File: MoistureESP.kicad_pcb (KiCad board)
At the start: 2 copper layers, 106 parts, among them J1 Conn_01x02_Pin, J2 Conn_MoisturePCB, J3 Conn_DS18B20, J4 Conn_01x06_Pin, J5 Conn_01x03_Pin, J7 USB4110-GF-A, Q1 SSM6K513NU-LF, Q10 SI7137DP-T1-GE3, Q2 SSM6K513NU-LF, Q3 2N7002W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

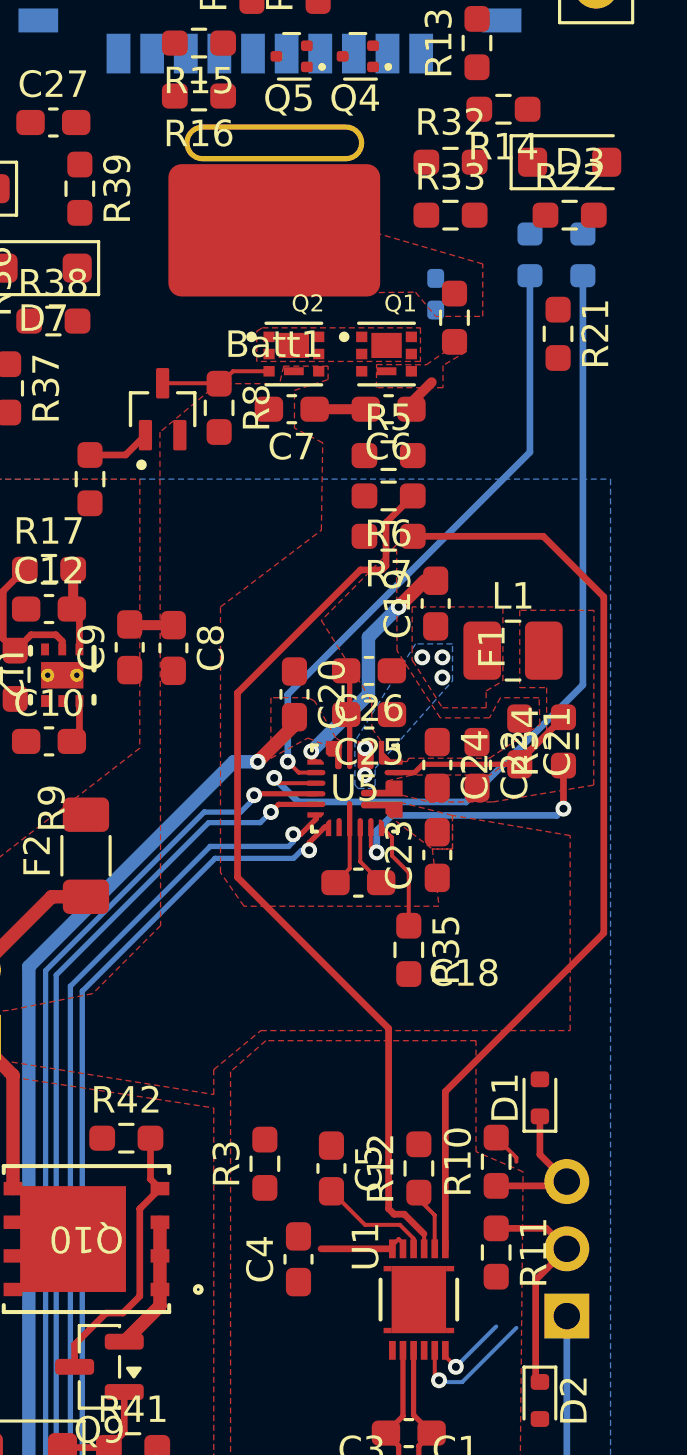
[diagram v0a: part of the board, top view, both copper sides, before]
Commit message: Fix BQ cell voltage wrong connection.
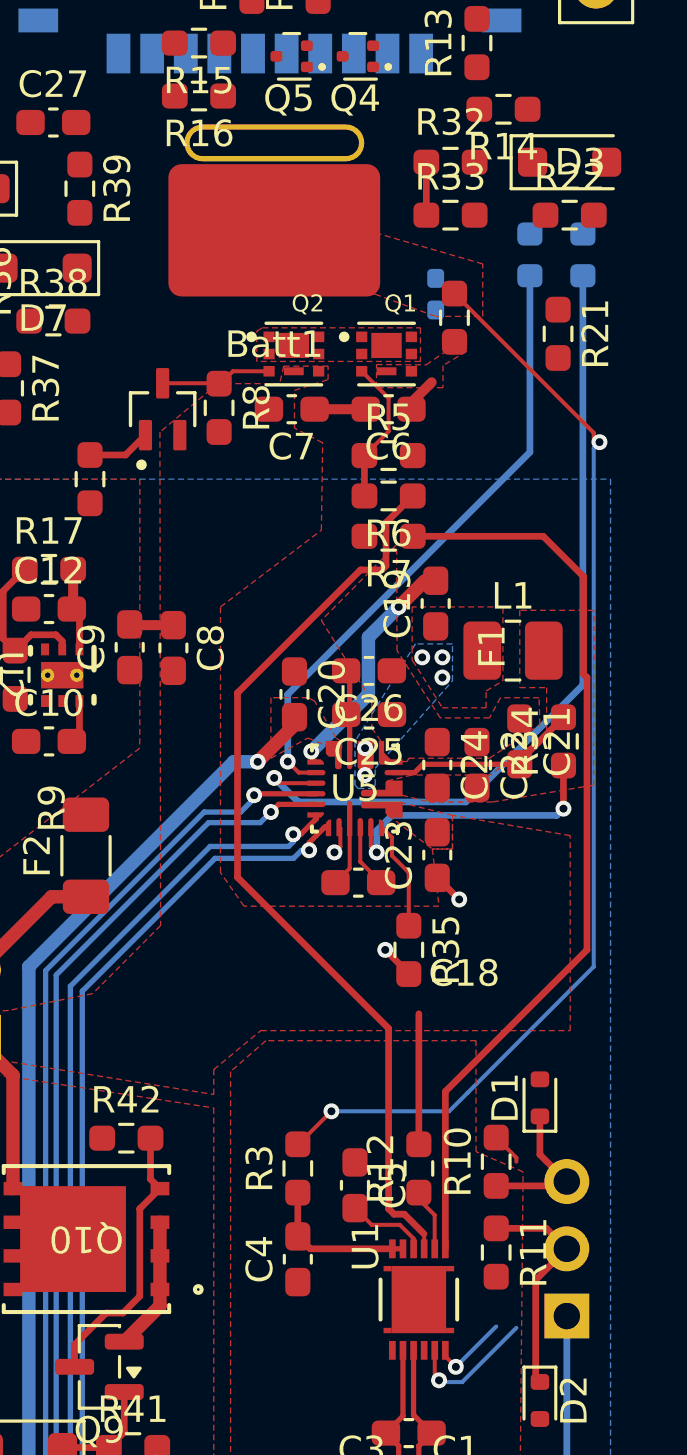
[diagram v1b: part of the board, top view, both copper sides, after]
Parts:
- moved R3 1.26 mm to (51.7, 114.9)
- moved C5 1.09 mm to (53.8, 115.6)
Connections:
- R3 pad 2: Net-(C6-Pad1) -> /battery/Vcell+
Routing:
- net /battery/Vcell+: track 0.00 -> 41.9 mm, vias 0 -> 2
- net Net-(Q1-Pad3): track 0.00 -> 5.51 mm
- net /charger/VBat: track 6.26 -> 11.2 mm
- net GNDPWR: track 14.5 -> 18.0 mm, vias 3 -> 6
- net Net-(U1-VC1): track 3.60 -> 6.16 mm
- net Vsys: track 5.21 -> 7.21 mm
- net Net-(U1-PBI): track 4.23 -> 3.08 mm
- net Net-(U1-DSG): track 35.3 -> 34.7 mm

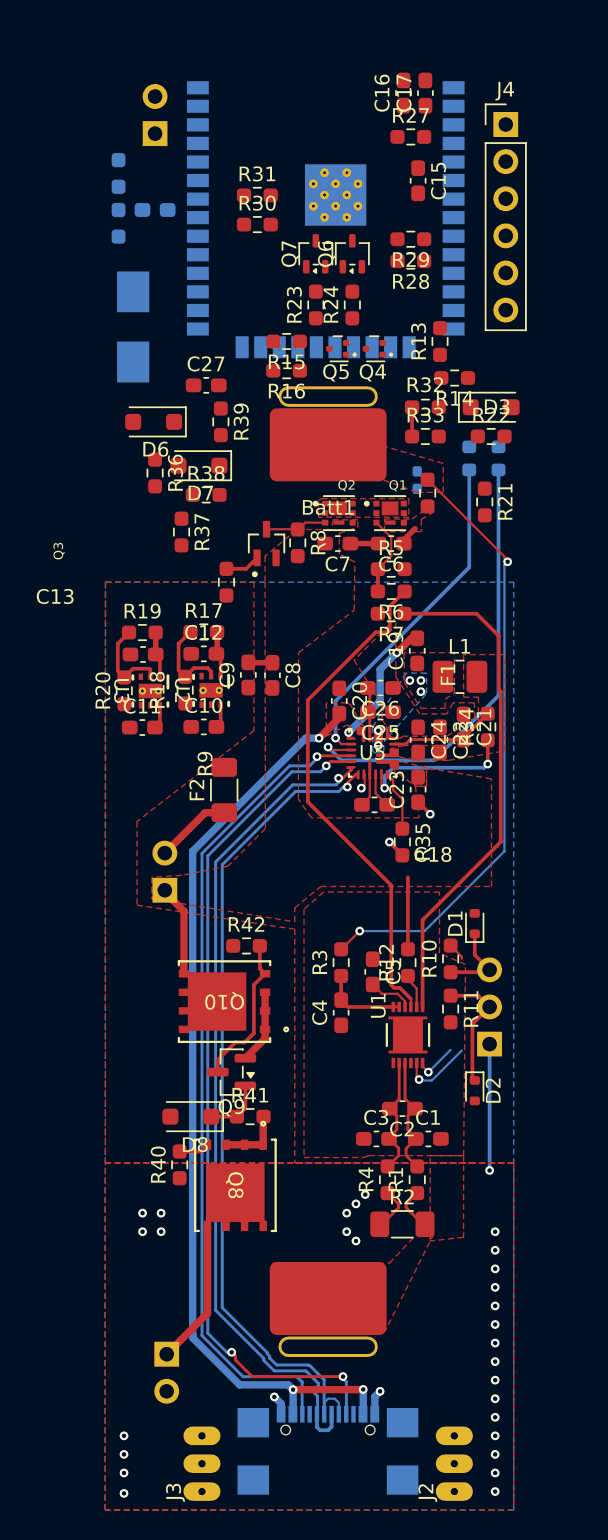
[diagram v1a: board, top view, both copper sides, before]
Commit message: Change USB charger position, redraw the zones.
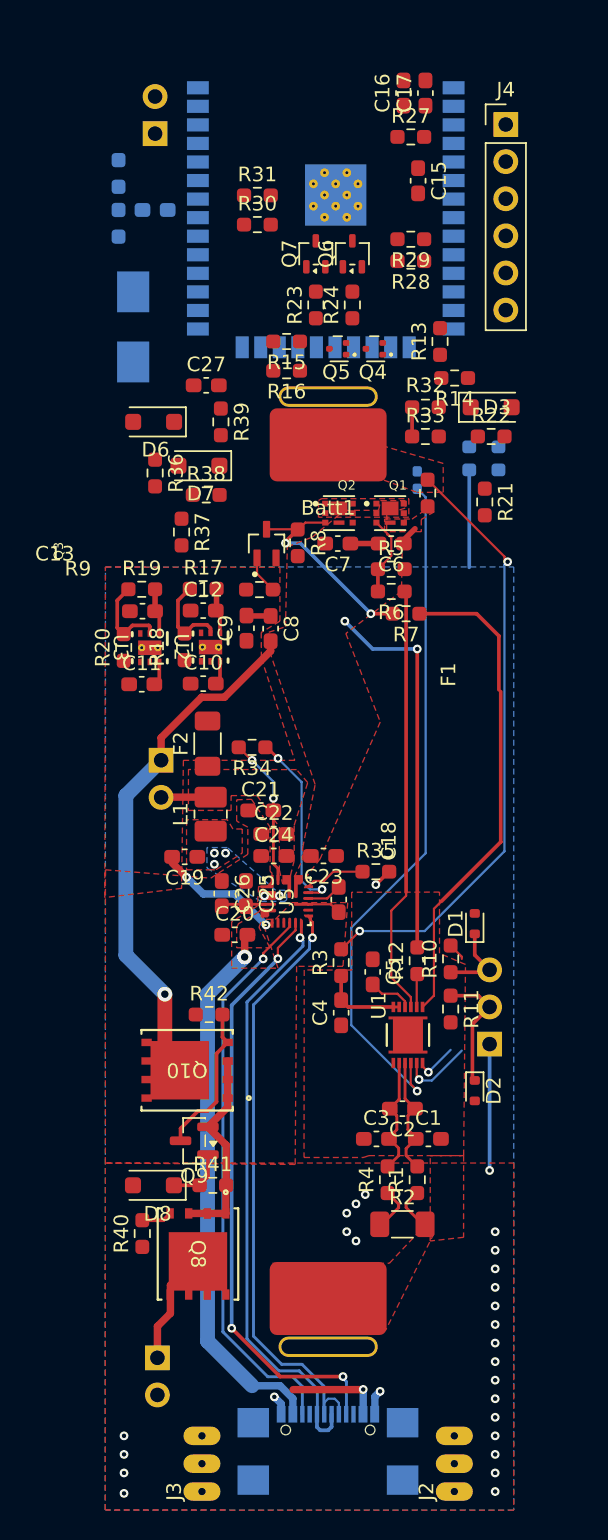
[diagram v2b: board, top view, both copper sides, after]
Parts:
- moved C19 21.3 mm to (41.0, 107.7), turned to 180 degrees
- moved L1 19.5 mm to (42.8, 104.8), turned to 90 degrees
- moved C26 17.8 mm to (43.5, 110.2), turned to -90 degrees
- moved C20 17.5 mm to (44.4, 113.0), turned to 0 degrees
- moved R34 16.2 mm to (45.6, 100.2), turned to 180 degrees
- moved C25 15.5 mm to (45.2, 110.2), turned to -90 degrees
- moved C21 15.0 mm to (46.2, 104.5), turned to 0 degrees
- moved C22 13.1 mm to (47.1, 106.1), turned to 0 degrees
- moved C24 12.7 mm to (47.1, 107.6), turned to 0 degrees
- moved U5 11.7 mm to (48.0, 110.7), turned to 90 degrees
- moved JP1 8.90 mm to (39.4, 101.1), turned to 180 degrees
- moved C23 7.91 mm to (50.5, 107.6), turned to 180 degrees
- moved C18 6.93 mm to (51.5, 110.6), turned to -90 degrees
- moved D8 5.35 mm to (38.8, 130.2)
- moved R40 5.35 mm to (38.1, 133.5)
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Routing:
- net /charger/VBat: track 11.2 -> 62.0 mm, vias 0 -> 3
- net Net-(U1-TS1): track 0.00 -> 47.5 mm, vias 0 -> 1
- net Net-(D4-K): track 31.0 -> 0.00 mm, vias 1 -> 0
- net VBUS: track 63.5 -> 43.9 mm, vias 3 -> 2
- net /charger/CC2: track 56.5 -> 38.8 mm
- net /charger/CC1: track 58.1 -> 41.0 mm
- net /charger/~{INOK}: track 23.4 -> 6.66 mm, vias 1 -> 0
- net /charger/DP1: track 58.5 -> 42.7 mm
- net /charger/DN1: track 56.3 -> 41.6 mm
- net Net-(Q2-Pad3): track 4.22 -> 14.8 mm, vias 0 -> 2
- net Net-(U1-CHG): track 34.8 -> 29.5 mm
- net Net-(Q9-E): track 9.54 -> 14.1 mm
- net /charger/PVL: track 7.36 -> 10.4 mm, vias 0 -> 2
- net GNDPWR: track 18.0 -> 15.7 mm, vias 6 -> 4
- net /auxchgr_prot/Vin+: track 9.94 -> 7.82 mm
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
